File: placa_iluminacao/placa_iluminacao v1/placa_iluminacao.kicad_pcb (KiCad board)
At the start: 2 copper layers, 11 parts

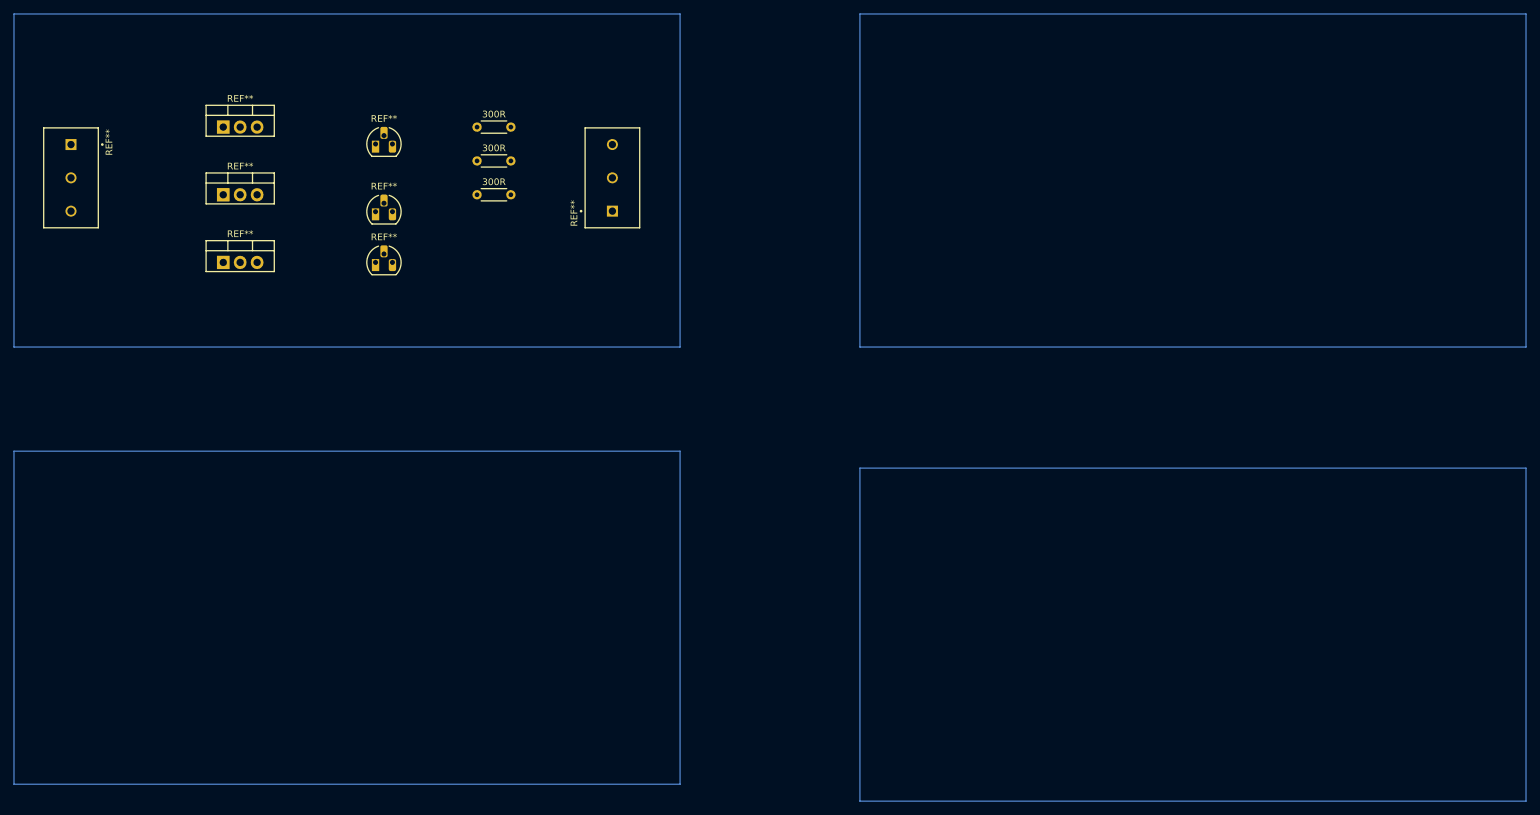
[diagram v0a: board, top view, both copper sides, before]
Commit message: Add PCB de iluminacao finalizada
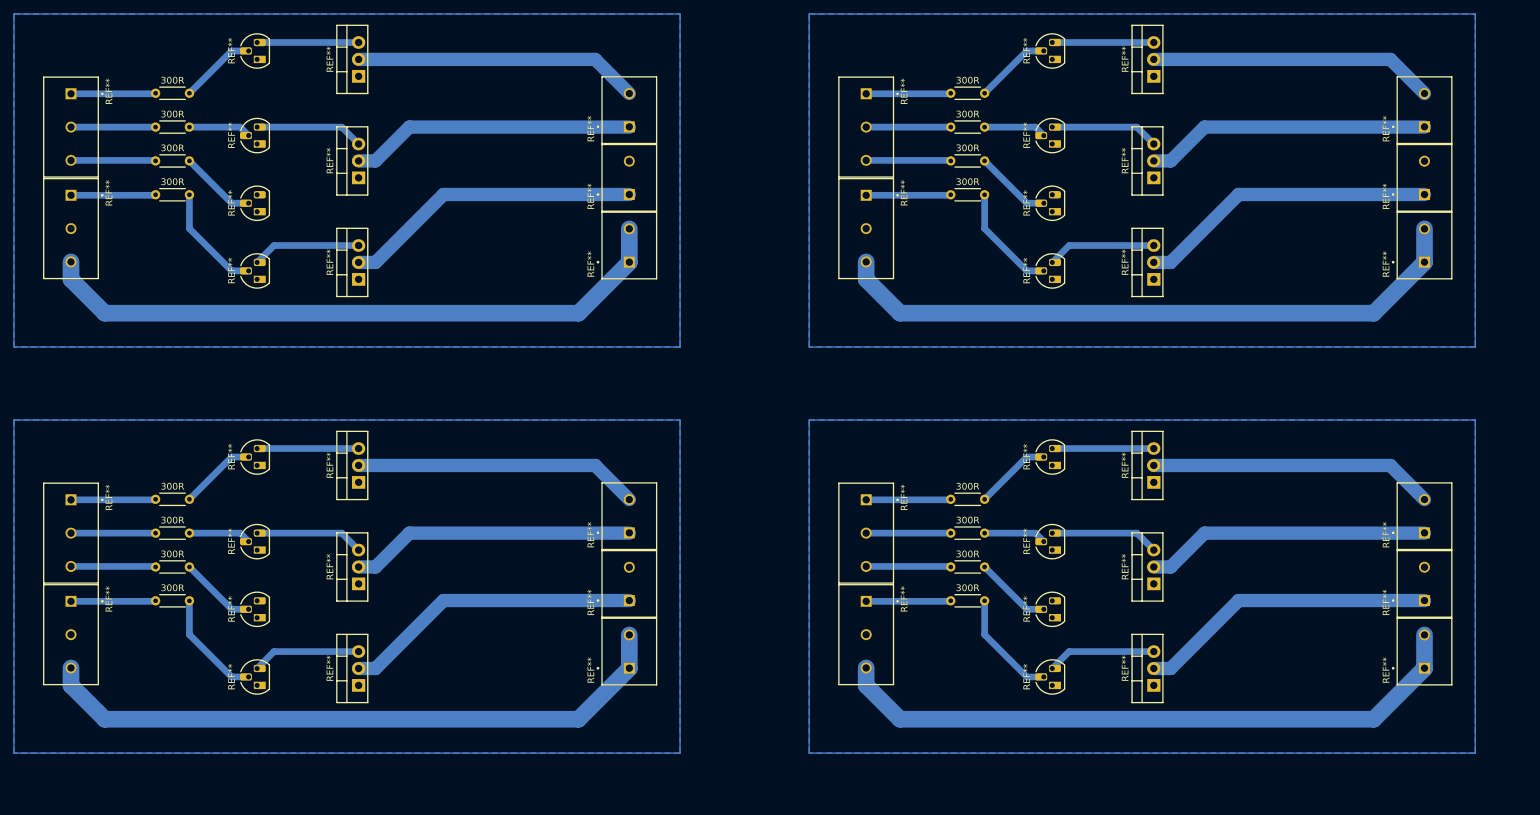
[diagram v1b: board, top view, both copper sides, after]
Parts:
- removed the REF** at (119.4, 53.3)
- added 300R: R_Axial_DIN0204_L3.6mm_D1.6mm_P5.08mm_Horizontal, Resistor_THT:R_Axial_DIN0204_L3.6mm_D1.6mm_P5.08mm_Horizontal, F.Cu at (170.2, 55.9)
- added 300R: R_Axial_DIN0204_L3.6mm_D1.6mm_P5.08mm_Horizontal, Resistor_THT:R_Axial_DIN0204_L3.6mm_D1.6mm_P5.08mm_Horizontal, F.Cu at (50.8, 101.6)
- added 300R: R_Axial_DIN0204_L3.6mm_D1.6mm_P5.08mm_Horizontal, Resistor_THT:R_Axial_DIN0204_L3.6mm_D1.6mm_P5.08mm_Horizontal, F.Cu at (170.2, 45.7)
- added 300R: R_Axial_DIN0204_L3.6mm_D1.6mm_P5.08mm_Horizontal, Resistor_THT:R_Axial_DIN0204_L3.6mm_D1.6mm_P5.08mm_Horizontal, F.Cu at (50.8, 40.6)
- added 300R: R_Axial_DIN0204_L3.6mm_D1.6mm_P5.08mm_Horizontal, Resistor_THT:R_Axial_DIN0204_L3.6mm_D1.6mm_P5.08mm_Horizontal, F.Cu at (170.2, 101.6)
- added 300R: R_Axial_DIN0204_L3.6mm_D1.6mm_P5.08mm_Horizontal, Resistor_THT:R_Axial_DIN0204_L3.6mm_D1.6mm_P5.08mm_Horizontal, F.Cu at (170.2, 111.8)
- added 300R: R_Axial_DIN0204_L3.6mm_D1.6mm_P5.08mm_Horizontal, Resistor_THT:R_Axial_DIN0204_L3.6mm_D1.6mm_P5.08mm_Horizontal, F.Cu at (170.2, 116.8)
- added 300R: R_Axial_DIN0204_L3.6mm_D1.6mm_P5.08mm_Horizontal, Resistor_THT:R_Axial_DIN0204_L3.6mm_D1.6mm_P5.08mm_Horizontal, F.Cu at (50.8, 106.7)
- added 300R: R_Axial_DIN0204_L3.6mm_D1.6mm_P5.08mm_Horizontal, Resistor_THT:R_Axial_DIN0204_L3.6mm_D1.6mm_P5.08mm_Horizontal, F.Cu at (170.2, 50.8)
- added 300R: R_Axial_DIN0204_L3.6mm_D1.6mm_P5.08mm_Horizontal, Resistor_THT:R_Axial_DIN0204_L3.6mm_D1.6mm_P5.08mm_Horizontal, F.Cu at (50.8, 111.8)
- added 300R: R_Axial_DIN0204_L3.6mm_D1.6mm_P5.08mm_Horizontal, Resistor_THT:R_Axial_DIN0204_L3.6mm_D1.6mm_P5.08mm_Horizontal, F.Cu at (50.8, 116.8)
- added 300R: R_Axial_DIN0204_L3.6mm_D1.6mm_P5.08mm_Horizontal, Resistor_THT:R_Axial_DIN0204_L3.6mm_D1.6mm_P5.08mm_Horizontal, F.Cu at (170.2, 106.7)
- added 300R: R_Axial_DIN0204_L3.6mm_D1.6mm_P5.08mm_Horizontal, Resistor_THT:R_Axial_DIN0204_L3.6mm_D1.6mm_P5.08mm_Horizontal, F.Cu at (170.2, 40.6)
- added REF**: TO-220-3_Vertical, Package_TO_SOT_THT:TO-220-3_Vertical, F.Cu at (200.7, 114.3)
- added REF**: TO-92L_HandSolder, Package_TO_SOT_THT:TO-92L_HandSolder, F.Cu at (66.0, 119.4)
- added REF**: TO-220-3_Vertical, Package_TO_SOT_THT:TO-220-3_Vertical, F.Cu at (81.3, 99.1)
- added REF**: TO-220-3_Vertical, Package_TO_SOT_THT:TO-220-3_Vertical, F.Cu at (200.7, 38.1)
- added REF**: TO-92L_HandSolder, Package_TO_SOT_THT:TO-92L_HandSolder, F.Cu at (185.4, 35.6)
- added REF**: TE_1546216-2, 1546216-2:TE_1546216-2, F.Cu at (241.3, 53.3)
- added REF**: TO-92L_HandSolder, Package_TO_SOT_THT:TO-92L_HandSolder, F.Cu at (185.4, 48.3)
- added REF**: TO-92L_HandSolder, Package_TO_SOT_THT:TO-92L_HandSolder, F.Cu at (66.0, 129.5)
- added REF**: TO-92L_HandSolder, Package_TO_SOT_THT:TO-92L_HandSolder, F.Cu at (185.4, 58.4)
- added REF**: TE_1546216-3, 1546216-3:TE_1546216-3, F.Cu at (157.5, 121.9)
- added REF**: TO-92L_HandSolder, Package_TO_SOT_THT:TO-92L_HandSolder, F.Cu at (185.4, 68.6)
- added REF**: TO-92L_HandSolder, Package_TO_SOT_THT:TO-92L_HandSolder, F.Cu at (66.0, 96.5)
- added REF**: TE_1546216-2, 1546216-2:TE_1546216-2, F.Cu at (121.9, 53.3)
- added REF**: TE_1546216-2, 1546216-2:TE_1546216-2, F.Cu at (241.3, 63.5)
- added REF**: TO-92L_HandSolder, Package_TO_SOT_THT:TO-92L_HandSolder, F.Cu at (66.0, 109.2)
- added REF**: TE_1546216-3, 1546216-3:TE_1546216-3, F.Cu at (38.1, 45.7)
- added REF**: TO-220-3_Vertical, Package_TO_SOT_THT:TO-220-3_Vertical, F.Cu at (200.7, 68.6)
- added REF**: TE_1546216-3, 1546216-3:TE_1546216-3, F.Cu at (38.1, 121.9)
- added REF**: TO-92L_HandSolder, Package_TO_SOT_THT:TO-92L_HandSolder, F.Cu at (185.4, 109.2)
- added REF**: TE_1546216-2, 1546216-2:TE_1546216-2, F.Cu at (121.9, 124.5)
- added REF**: TO-92L_HandSolder, Package_TO_SOT_THT:TO-92L_HandSolder, F.Cu at (185.4, 129.5)
- added REF**: TE_1546216-2, 1546216-2:TE_1546216-2, F.Cu at (241.3, 104.1)
- added REF**: TE_1546216-2, 1546216-2:TE_1546216-2, F.Cu at (121.9, 104.1)
- added REF**: TE_1546216-2, 1546216-2:TE_1546216-2, F.Cu at (241.3, 43.2)
- added REF**: TE_1546216-2, 1546216-2:TE_1546216-2, F.Cu at (121.9, 114.3)
- added REF**: TE_1546216-2, 1546216-2:TE_1546216-2, F.Cu at (241.3, 124.5)
- added REF**: TO-92L_HandSolder, Package_TO_SOT_THT:TO-92L_HandSolder, F.Cu at (185.4, 119.4)
- added REF**: TE_1546216-2, 1546216-2:TE_1546216-2, F.Cu at (121.9, 43.2)
- added REF**: TO-220-3_Vertical, Package_TO_SOT_THT:TO-220-3_Vertical, F.Cu at (200.7, 53.3)
- added REF**: TO-92L_HandSolder, Package_TO_SOT_THT:TO-92L_HandSolder, F.Cu at (66.0, 35.6)
- added REF**: TO-220-3_Vertical, Package_TO_SOT_THT:TO-220-3_Vertical, F.Cu at (200.7, 129.5)
- added REF**: TE_1546216-2, 1546216-2:TE_1546216-2, F.Cu at (241.3, 114.3)
- added REF**: TO-220-3_Vertical, Package_TO_SOT_THT:TO-220-3_Vertical, F.Cu at (81.3, 114.3)
- added REF**: TE_1546216-3, 1546216-3:TE_1546216-3, F.Cu at (157.5, 45.7)
- added REF**: TE_1546216-2, 1546216-2:TE_1546216-2, F.Cu at (121.9, 63.5)
- added REF**: TO-92L_HandSolder, Package_TO_SOT_THT:TO-92L_HandSolder, F.Cu at (185.4, 96.5)
- added REF**: TE_1546216-3, 1546216-3:TE_1546216-3, F.Cu at (157.5, 106.7)
- added REF**: TE_1546216-3, 1546216-3:TE_1546216-3, F.Cu at (157.5, 61.0)
- added REF**: TE_1546216-3, 1546216-3:TE_1546216-3, F.Cu at (38.1, 106.7)
- added REF**: TO-220-3_Vertical, Package_TO_SOT_THT:TO-220-3_Vertical, F.Cu at (81.3, 129.5)
- added REF**: TO-220-3_Vertical, Package_TO_SOT_THT:TO-220-3_Vertical, F.Cu at (200.7, 99.1)
- moved 300R 48.3 mm to (50.8, 55.9)
- moved 300R 48.3 mm to (50.8, 45.7)
- moved 300R 48.3 mm to (50.8, 50.8)
- moved REF** 21.7 mm to (81.3, 38.1), turned to 90 degrees
- moved REF** 20.5 mm to (81.3, 68.6), turned to 90 degrees
- moved REF** 20.5 mm to (81.3, 53.3), turned to 90 degrees
- moved REF** 18.0 mm to (66.0, 68.6), turned to 90 degrees
- moved REF** 17.8 mm to (66.0, 48.3), turned to 90 degrees
- moved REF** 17.8 mm to (66.0, 58.4), turned to 90 degrees
- moved REF** 7.62 mm to (38.1, 61.0)
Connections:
- REF** pad 1: (no net) -> GND (x5)
- REF** pad 2: (no net) -> GND
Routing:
- net (no net): track 0.00 -> 1499.6 mm
- added copper zone on B.Cu, net GND
